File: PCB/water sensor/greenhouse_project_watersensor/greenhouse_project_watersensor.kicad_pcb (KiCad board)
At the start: 2 copper layers, 40 x 59.1 mm, 29 parts, among them J1 Conn_01x09_Socket, J3 Conn_01x10_Socket, Q1 BC847, Q2 BC847, Q3 BC847, Q4 BC847, Q5 BC847, Q6 BC847, Q7 BC847, Q8 BC847

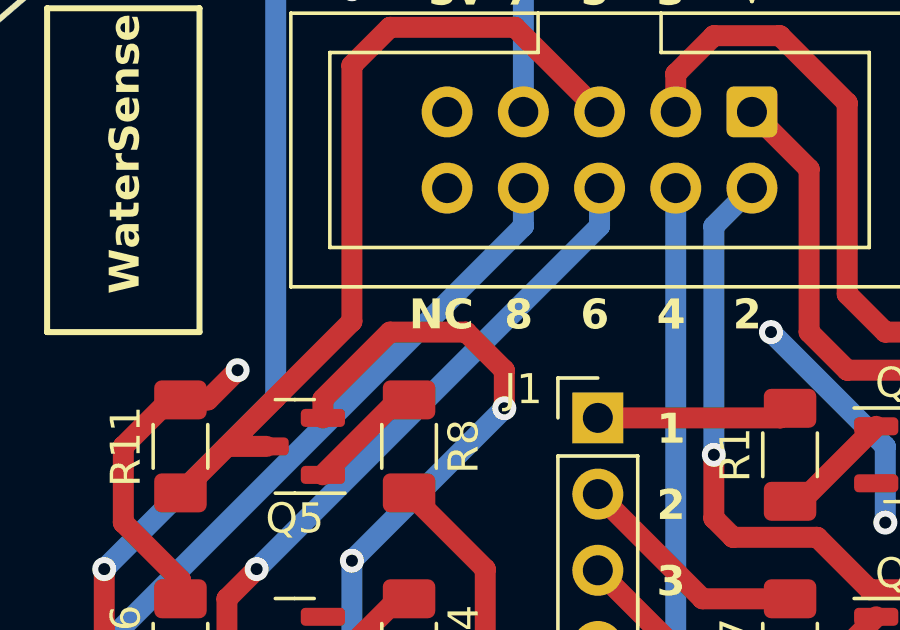
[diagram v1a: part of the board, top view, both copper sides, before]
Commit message: Uploaded finals
Pushed the final versions of the microcontroller code, Nodered code, PCB and CAD files to the repository
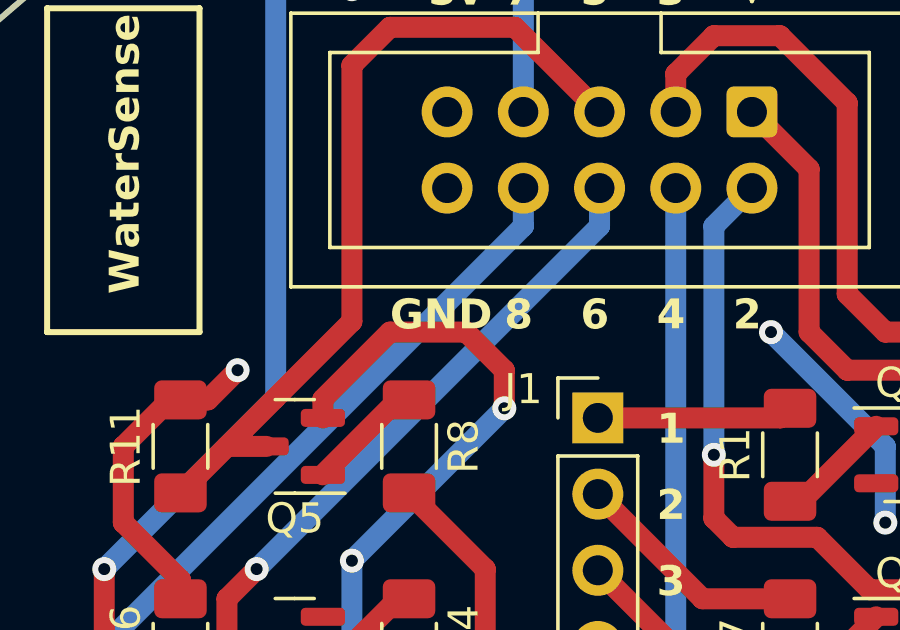
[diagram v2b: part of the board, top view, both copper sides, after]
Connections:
- J3 pad 10: unconnected-(J3-Pin_10-Pad10) -> GNDREF
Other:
- board text added: "GND"
- board text removed: "NC"
